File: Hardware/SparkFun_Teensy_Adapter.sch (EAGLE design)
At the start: 18 parts, among them J1 ARDUINO_R3_SHIELDUNO_R3_SHIEL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, J2 AVR_SPI_PRG_6PTH, U1 TEENSY-3.1

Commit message: Adding switch for USB Host, RTC battery holder
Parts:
- removed J2: AVR_SPI_PRG_6PTH, SparkFun-Connectors:AVR_SPI_PRG_6PTH
- removed U2: (no value), SparkFun-PowerIC:MIC52055V
- added BAT1: (no value), SparkFun-Electromechanical:BATTERY12PTH
- added C2: 100uF, SparkFun-Capacitors:100UF6.3V20%(1210)
- added JP1: M02PTH, SparkFun-Connectors:M02PTH
- added JP11: TEENSY-3.1, Testing:TEENSY-3.1
- added S1: (no value), SparkFun-Electromechanical:SWITCH-SPDTPTH
- JP9: value (none) -> AVR_SPI_PRG_6PTH; device SparkFun-Connectors:M03PTH -> SparkFun-Connectors:AVR_SPI_PRG_6PTH
- U1: value TEENSY-3.1 -> (none); device Testing:TEENSY-3.1 -> SparkFun-PowerIC:MIC52055V
- renumbered J1 to JP10
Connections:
- new net N$1: C2.1, S1.S
- net 3.3V: now also JP11.3.3V, JP9.2; no longer J2.2, U1.3.3V
- net 5V: now also JP11.VIN, U1.OUT; no longer U1.VIN, U2.OUT
- net A0: now also JP11.A0/14; no longer U1.A0/14
- net A1: now also JP11.A1/15; no longer U1.A1/15
- net A10: now also JP11.A10; no longer U1.A10
- net A11: now also JP11.A11; no longer U1.A11
- net A14/DAC: now also JP11.A14/DAC, JP8.2; no longer JP8.4, U1.A14/DAC
- net A2: now also JP11.A2/16; no longer U1.A2/16
- net A3: now also JP11.A3/17; no longer U1.A3/17
- net A6: now also JP11.A6/20*; no longer U1.A6/20*
- net A7: now also JP11.A7/21*; no longer U1.A7/21*
- net A8: now also JP11.A8/22*; no longer U1.A8/22*
- net A9: now also JP11.A9/23*; no longer U1.A9/23*
- net AREF: now also JP1.2, JP11.AREF; no longer JP9.3, U1.AREF
- net CS: now also JP11.10*/TX2/CS; no longer U1.10*/TX2/CS
- net D2: now also JP11.2; no longer U1.2
- net D3: now also JP11.3*; no longer U1.3*
- net D4: now also JP11.4*; no longer U1.4*
- net D5: now also JP11.5*; no longer U1.5*
- net D6: now also JP11.6*; no longer U1.6*
- net D7: now also JP11.7/RX3; no longer U1.7/RX3
- net D8: now also JP11.8/TX3; no longer U1.8/TX3
- net D9: now also JP11.9*/RX2; no longer U1.9*/RX2
- net GND: now also BAT1.+, C2.2, JP1.1, JP11.AGND, JP11.GND, JP11.GND1, JP8.4, JP9.6; no longer J2.6, JP9.1, U1.AGND, U1.GND1, U2.GND
- net MISO: now also JP11.12/DIN, JP9.1; no longer J2.1, U1.12/DIN
- net MOSI: now also JP11.11/DOUT, JP9.4; no longer J2.4, U1.11/DOUT
- net PROG: now also JP11.PROG; no longer U1.PROG
- net RESET: now also JP9.5; no longer J2.5
- net RTC_BATT: now also BAT1.-, JP11.VBAT; no longer JP8.2, U1.VBAT
- net RX: now also JP11.0/RX1; no longer U1.0/RX1
- net SCK: now also JP11.13/SCK, JP9.3; no longer J2.3, U1.13/SCK
- net SCL: now also JP11.A5/19/SCL0; no longer U1.A5/19/SCL0
- net SDA: now also JP11.A4/18/SDA0; no longer U1.A4/18/SDA0
- net TX: now also JP11.1/TX1; no longer U1.1/TX1
- net VRAW: now also U1.EN, U1.IN; no longer U2.EN, U2.IN
- net VUSB: now also JP11.VUSB, S1.P; no longer JP9.2, U1.VUSB
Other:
- note added: "ADC/PROG"
- note added: "RTC Battery"
- note added: "Switch to select USB Host mode"
- note added: "VBUS"
- note removed: "AREF/VBUS"
- note removed: "Add 100uF Cap for USB Host applications."
- note removed: "RTC Clock/ADC/PROG"
- moved on the sheet: C1, JP2, JP3

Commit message: Swapping to all PTH parts, fixing name silk
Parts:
- C1: device SparkFun-Capacitors:10UF-16V-10%(TANT) -> SparkFun-Capacitors:10UF-25V-20%(PTH)
- C2: device SparkFun-Capacitors:100UF6.3V20%(1210) -> SparkFun-Capacitors:100UF-25V-20%(PTH)
- U1: value (none) -> 5V; device SparkFun-PowerIC:MIC52055V -> SparkFun-PowerIC:V_REG_78XX-TO-220
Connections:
- net GND: now also C2.-; no longer C2.2
- net N$1: now also C2.+; no longer C2.1
- net VRAW: no longer U1.EN
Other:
- note added: "Toni Klopfenstein"
- note added: "v01"
- note removed: "5V"
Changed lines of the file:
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@@
 <layer number="223" name="223bmp" color="24" fill="1" visible="no" active="no"/>
 <layer number="224" name="224bmp" color="25" fill="1" visible="no" active="no"/>
+<layer number="225" name="225bmp" color="7" fill="1" visible="yes" active="yes"/>
+<layer number="226" name="226bmp" color="7" fill="1" visible="yes" active="yes"/>
+<layer number="227" name="227bmp" color="7" fill="1" visible="yes" active="yes"/>
+<layer number="228" name="228bmp" color="7" fill="1" visible="yes" active="yes"/>
+<layer number="229" name="229bmp" color="7" fill="1" visible="yes" active="yes"/>
+<layer number="230" name="230bmp" color="7" fill="1" visible="yes" active="yes"/>
+<layer number="231" name="231bmp" color="7" fill="1" visible="yes" active="yes"/>
 <layer number="248" name="Housing" color="7" fill="1" visible="yes" active="yes"/>
 <layer number="249" name="Edge" color="7" fill="1" visible="yes" active="yes"/>
@@
 <layer number="255" name="routoute" color="7" fill="1" visible="yes" active="yes"/>
 </layers>
-<schematic xreflabel="%F%N/%S" xrefpart="/%S.%C%R">
+<schematic xreflabel="%F%N/%S" xrefpart="/%S">
 <attributes>
 </attributes>
@@
 <part name="JP2" library="SparkFun-Connectors" deviceset="POWER_JACK" device="PTH_LOCK"/>
 <part name="GND5" library="SparkFun-Aesthetics" deviceset="GND" device=""/>
-<part name="U1" library="SparkFun-PowerIC" deviceset="MIC5205" device="5V"/>
 <part name="JP3" library="SparkFun-Connectors" deviceset="M02" device="JST-PTH-2"/>
 <part name="GND6" library="SparkFun-Aesthetics" deviceset="GND" device=""/>
 <part name="GND7" library="SparkFun-Aesthetics" deviceset="GND" device=""/>
-<part name="C1" library="SparkFun-Capacitors" deviceset="10UF-16V-10%(TANT)" device="" value="10uF"/>
+<part name="C1" library="SparkFun-Capacitors" deviceset="10UF-25V-20%(PTH)" device="" value="10uF"/>
 <part name="GND8" library="SparkFun-Aesthetics" deviceset="GND" device=""/>
 <part name="JP6" library="SparkFun-Connectors" deviceset="M02" device="PTH"/>
@@
 <part name="GND10" library="SparkFun-Aesthetics" deviceset="GND" device=""/>
 <part name="S1" library="SparkFun-Electromechanical" deviceset="SWITCH-SPDT" device="PTH"/>
-<part name="C2" library="SparkFun-Capacitors" deviceset="100UF6.3V20%(1210)" device="" value="100uF"/>
+<part name="U1" library="SparkFun-PowerIC" deviceset="V_REG_78XX" device="-TO-220" value="5V"/>
+<part name="C2" library="SparkFun-Capacitors" deviceset="100UF-25V-20%(PTH)" device="" value="100uF"/>
 </parts>
 <sheets>
@@
 <plain>
 <text x="10.16" y="157.48" size="1.778" layer="97">Input Voltage: 4-12V</text>
-<text x="76.2" y="139.7" size="1.778" layer="97">5V</text>
 <text x="218.44" y="182.88" size="1.27" layer="97">Switch to select USB Host mode</text>
 <text x="152.4" y="154.94" size="1.4224" layer="97">Add 32.768kHZ crystal to Teensy for use of RTC.  </text>
@@
 <wire x1="106.68" y1="185.42" x2="106.68" y2="127" width="0.2032" layer="97" style="shortdash"/>
 <text x="116.84" y="129.54" size="2.54" layer="97">RTC Battery</text>
+<text x="241.3" y="7.62" size="2.54" layer="94">v01</text>
+<text x="167.64" y="10.16" size="2.54" layer="94">Toni Klopfenstein</text>
 </plain>
 <instances>
@@
 </instance>
 <instance part="GND5" gate="1" x="40.64" y="137.16"/>
-<instance part="U1" gate="G$1" x="78.74" y="149.86"/>
 <instance part="JP3" gate="G$1" x="10.16" y="170.18" smashed="yes">
 <attribute name="NAME" x="7.62" y="176.022" size="1.778" layer="95"/>
 </instance>
 <instance part="GND6" gate="1" x="20.32" y="165.1"/>
-<instance part="GND7" gate="1" x="63.5" y="137.16"/>
+<instance part="GND7" gate="1" x="81.28" y="137.16"/>
 <instance part="C1" gate="G$1" x="50.8" y="149.86"/>
 <instance part="GND8" gate="1" x="50.8" y="137.16"/>
@@
 <instance part="GND10" gate="1" x="129.54" y="17.78"/>
 <instance part="S1" gate="1" x="213.36" y="177.8"/>
-<instance part="C2" gate="G$1" x="220.98" y="165.1"/>
+<instance part="U1" gate="G$1" x="81.28" y="154.94"/>
+<instance part="C2" gate="G$1" x="220.98" y="167.64"/>
 </instances>
 <busses>
@@
 </segment>
 <segment>
-<pinref part="U1" gate="G$1" pin="GND"/>
-<wire x1="68.58" y1="149.86" x2="63.5" y2="149.86" width="0.1524" layer="91"/>
-<wire x1="63.5" y1="149.86" x2="63.5" y2="139.7" width="0.1524" layer="91"/>
-<pinref part="GND7" gate="1" pin="GND"/>
-</segment>
-<segment>
 <pinref part="C1" gate="G$1" pin="-"/>
 <pinref part="GND8" gate="1" pin="GND"/>
@@
 <pinref part="GND11" gate="1" pin="GND"/>
 <wire x1="220.98" y1="162.56" x2="220.98" y2="160.02" width="0.1524" layer="91"/>
-<pinref part="C2" gate="G$1" pin="2"/>
+<pinref part="C2" gate="G$1" pin="-"/>
+</segment>
+<segment>
+<pinref part="GND7" gate="1" pin="GND"/>
+<wire x1="81.28" y1="144.78" x2="81.28" y2="142.24" width="0.1524" layer="91"/>
+<pinref part="U1" gate="G$1" pin="GND"/>
+<wire x1="81.28" y1="142.24" x2="81.28" y2="139.7" width="0.1524" layer="91"/>
+<wire x1="81.28" y1="147.32" x2="81.28" y2="144.78" width="0.1524" layer="91"/>
 </segment>
 </net>
@@
 <segment>
 <pinref part="JP2" gate="G$1" pin="PWR"/>
-<pinref part="U1" gate="G$1" pin="IN"/>
 <wire x1="22.86" y1="154.94" x2="50.8" y2="154.94" width="0.1524" layer="91"/>
-<pinref part="U1" gate="G$1" pin="EN"/>
-<wire x1="50.8" y1="154.94" x2="60.96" y2="154.94" width="0.1524" layer="91"/>
-<wire x1="60.96" y1="154.94" x2="68.58" y2="154.94" width="0.1524" layer="91"/>
-<wire x1="68.58" y1="144.78" x2="60.96" y2="144.78" width="0.1524" layer="91"/>
-<wire x1="60.96" y1="144.78" x2="60.96" y2="154.94" width="0.1524" layer="91"/>
-<junction x="60.96" y="154.94"/>
+<wire x1="50.8" y1="154.94" x2="73.66" y2="154.94" width="0.1524" layer="91"/>
 <pinref part="C1" gate="G$1" pin="+"/>
 <wire x1="50.8" y1="152.4" x2="50.8" y2="154.94" width="0.1524" layer="91"/>
 <junction x="50.8" y="154.94"/>
+<pinref part="U1" gate="G$1" pin="IN"/>
 </segment>
 </net>
@@
 </segment>
 <segment>
-<pinref part="U1" gate="G$1" pin="OUT"/>
-<wire x1="86.36" y1="154.94" x2="91.44" y2="154.94" width="0.1524" layer="91"/>
-<label x="91.44" y="154.94" size="1.27" layer="95" xref="yes"/>
-</segment>
-<segment>
 <pinref part="JP10" gate="G$1" pin="5V"/>
 <wire x1="63.5" y1="86.36" x2="55.88" y2="86.36" width="0.1524" layer="91"/>
 <label x="55.88" y="86.36" size="1.27" layer="95" rot="R180" xref="yes"/>
+</segment>
+<segment>
+<wire x1="96.52" y1="154.94" x2="99.06" y2="154.94" width="0.1524" layer="91"/>
+<label x="101.6" y="154.94" size="1.27" layer="95" xref="yes"/>
+<pinref part="U1" gate="G$1" pin="OUT"/>
+<wire x1="99.06" y1="154.94" x2="101.6" y2="154.94" width="0.1524" layer="91"/>
+<wire x1="88.9" y1="154.94" x2="96.52" y2="154.94" width="0.1524" layer="91"/>
 </segment>
 </net>
@@
 <wire x1="218.44" y1="175.26" x2="220.98" y2="175.26" width="0.1524" layer="91"/>
 <wire x1="220.98" y1="175.26" x2="220.98" y2="170.18" width="0.1524" layer="91"/>
-<pinref part="C2" gate="G$1" pin="1"/>
-</segment>
-</net>
+<pinref part="C2" gate="G$1" pin="+"/>
+</segment>
+</net>

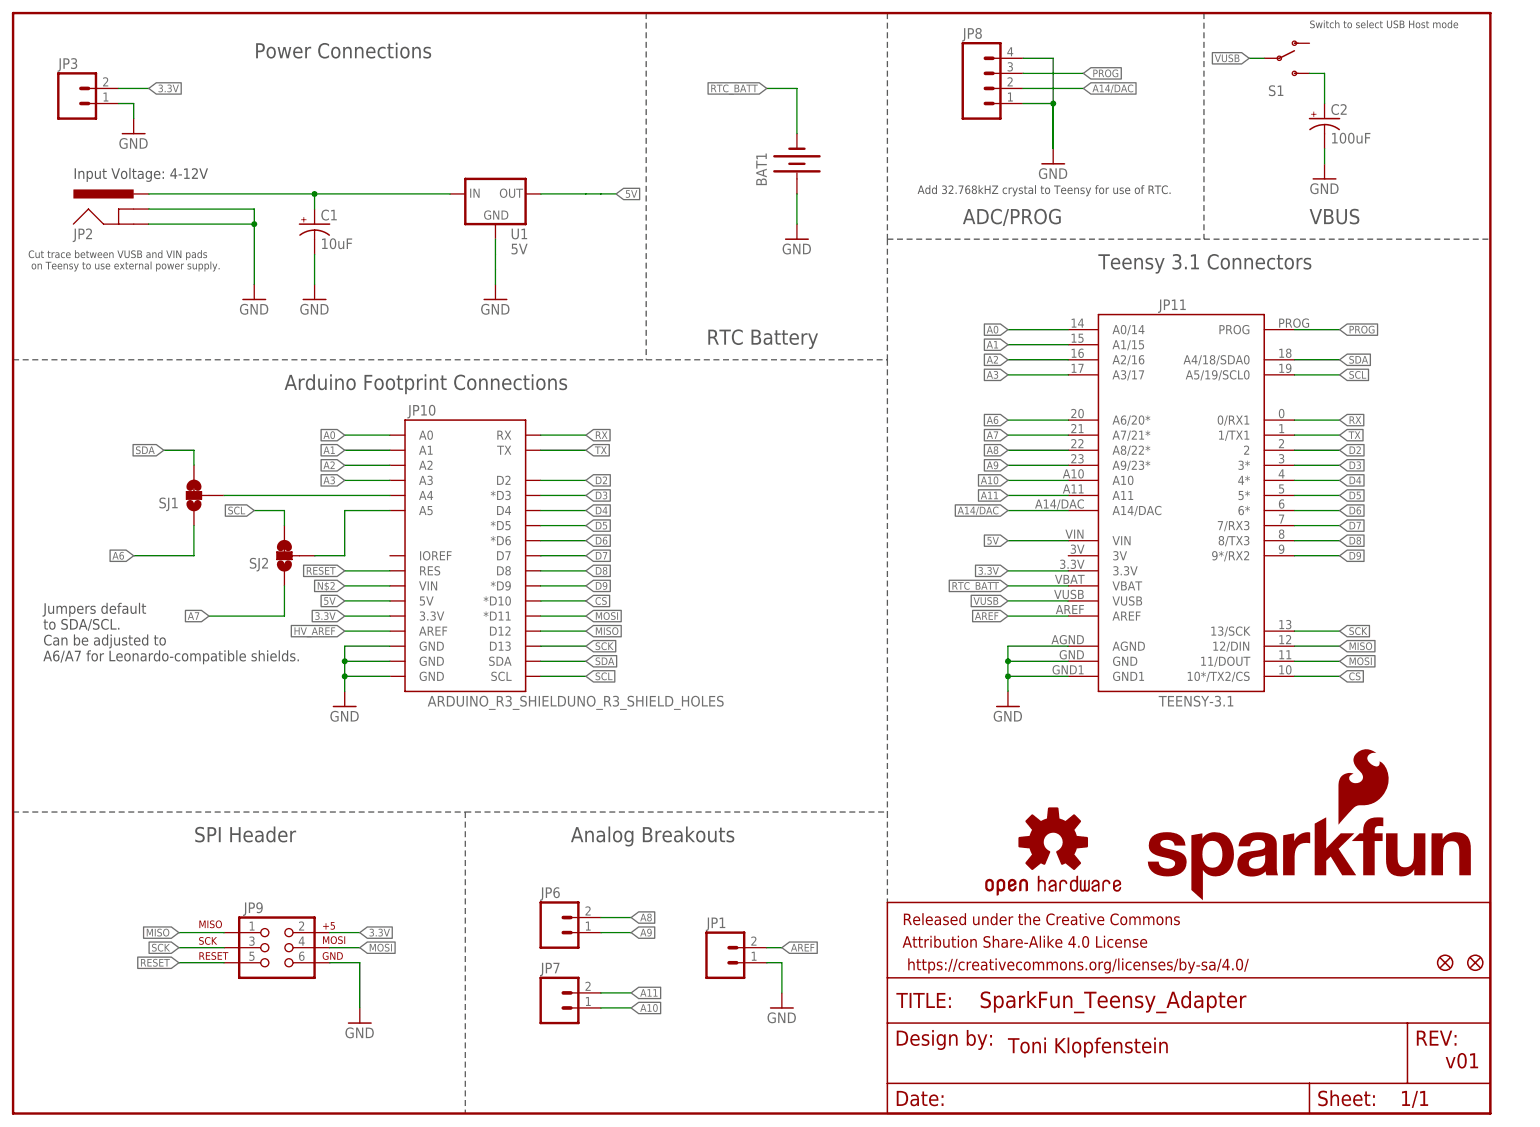
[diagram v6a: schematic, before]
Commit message: Fixing QC checklist issues
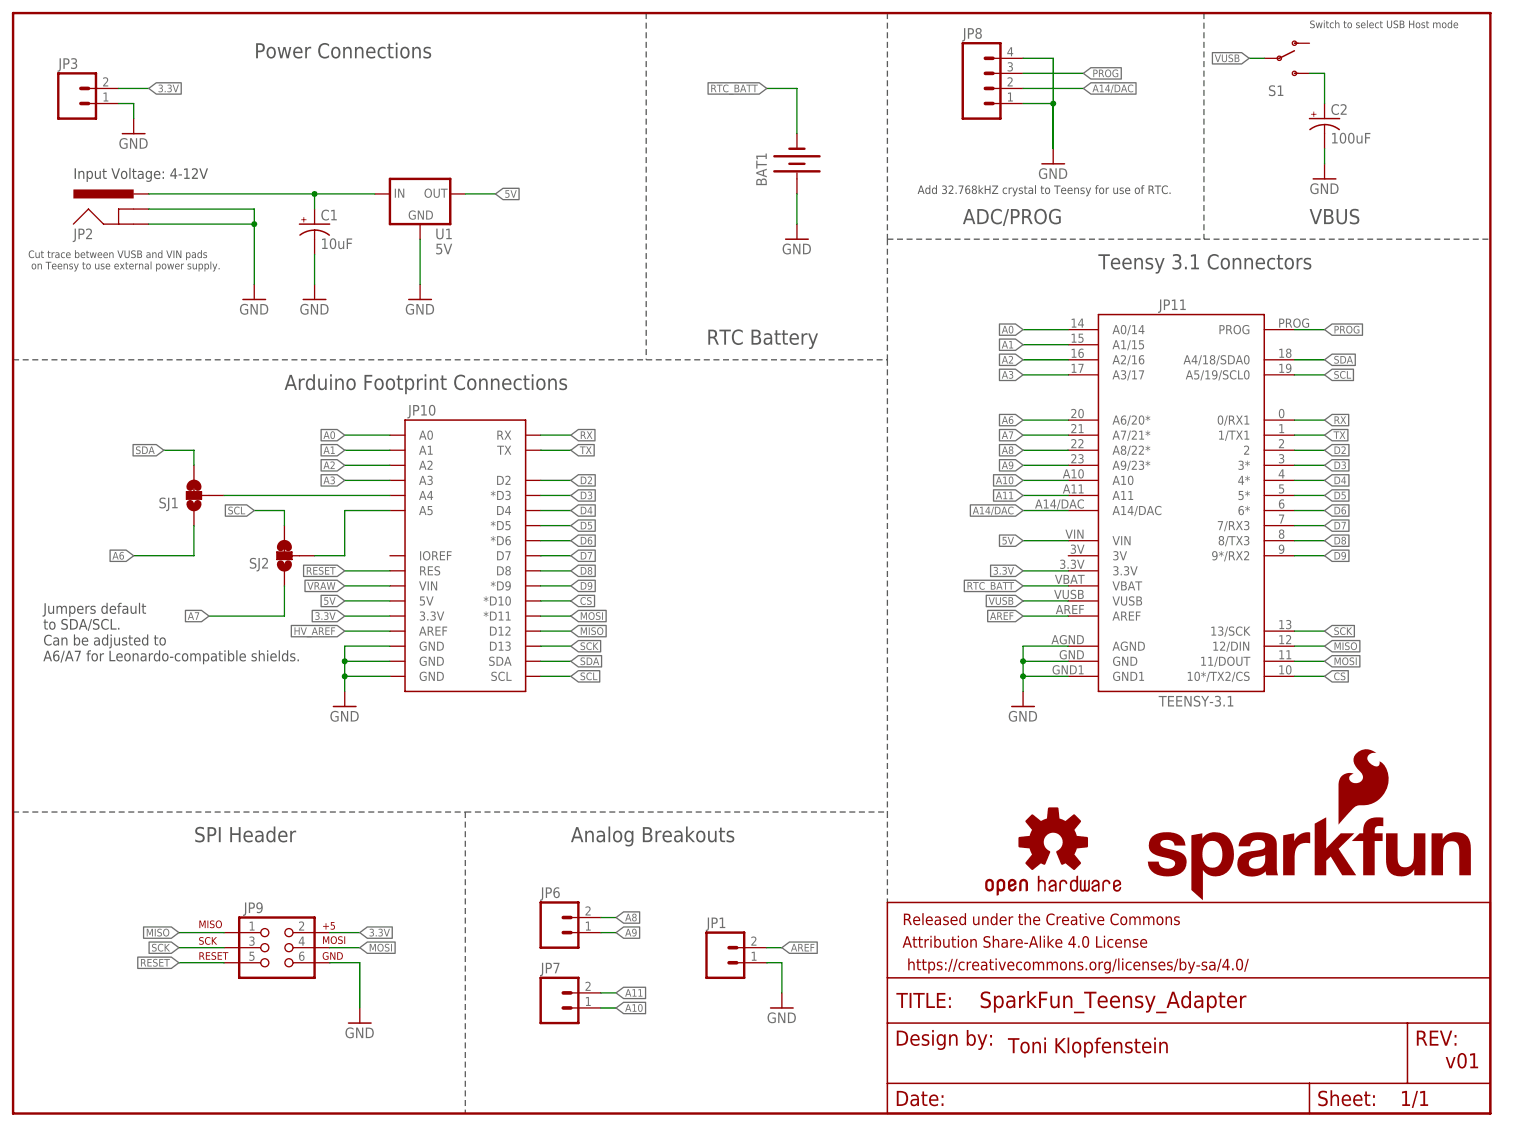
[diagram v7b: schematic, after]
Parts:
- removed FID1, FID2: FIDUCIAL1X2, SparkFun-Aesthetics:FIDUCIAL1X2
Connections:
- removed net N$2: JP10.VIN
- net VRAW: now also JP10.VIN
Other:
- moved on the sheet: U1

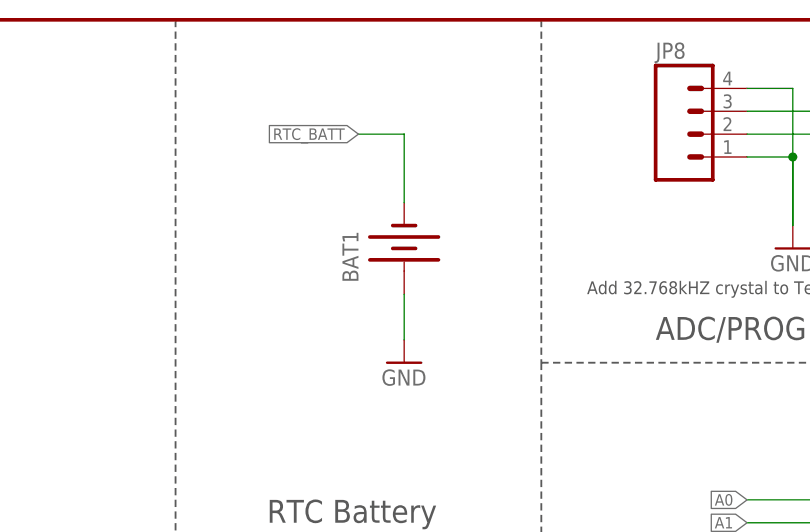
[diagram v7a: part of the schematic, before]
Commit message: Fixing battery connections
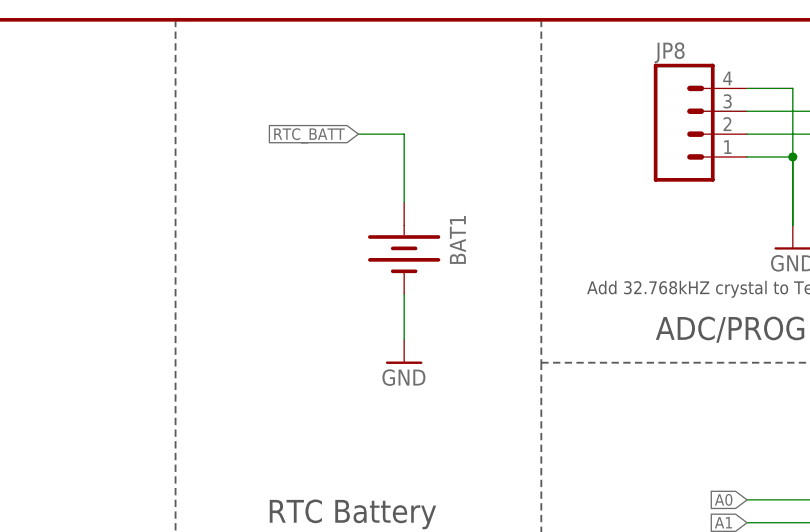
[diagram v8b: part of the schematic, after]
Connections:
- net GND: now also BAT1.-; no longer BAT1.+
- net RTC_BATT: now also BAT1.+; no longer BAT1.-
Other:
- moved on the sheet: BAT1
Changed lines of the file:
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@@
 <instance part="GND9" gate="1" x="175.26" y="160.02"/>
 <instance part="GND11" gate="1" x="220.98" y="157.48"/>
-<instance part="BAT1" gate="G$1" x="132.08" y="160.02" rot="R90"/>
+<instance part="BAT1" gate="G$1" x="132.08" y="160.02" rot="R270"/>
 <instance part="GND4" gate="1" x="132.08" y="147.32"/>
 <instance part="JP1" gate="G$1" x="119.38" y="25.4" smashed="yes">
@@
 </segment>
 <segment>
-<pinref part="BAT1" gate="G$1" pin="+"/>
-<pinref part="GND4" gate="1" pin="GND"/>
-<wire x1="132.08" y1="154.94" x2="132.08" y2="149.86" width="0.1524" layer="91"/>
-</segment>
-<segment>
 <pinref part="JP1" gate="G$1" pin="1"/>
 <wire x1="127" y1="25.4" x2="129.54" y2="25.4" width="0.1524" layer="91"/>
@@
 <pinref part="U1" gate="G$1" pin="GND"/>
 <wire x1="68.58" y1="147.32" x2="68.58" y2="139.7" width="0.1524" layer="91"/>
+</segment>
+<segment>
+<pinref part="BAT1" gate="G$1" pin="-"/>
+<pinref part="GND4" gate="1" pin="GND"/>
+<wire x1="132.08" y1="154.94" x2="132.08" y2="149.86" width="0.1524" layer="91"/>
 </segment>
 </net>
@@
 </segment>
 <segment>
-<pinref part="BAT1" gate="G$1" pin="-"/>
-<wire x1="132.08" y1="165.1" x2="132.08" y2="172.72" width="0.1524" layer="91"/>
 <wire x1="132.08" y1="172.72" x2="127" y2="172.72" width="0.1524" layer="91"/>
 <label x="127" y="172.72" size="1.27" layer="95" rot="R180" xref="yes"/>
-</segment>
-</net>
+<pinref part="BAT1" gate="G$1" pin="+"/>
+<wire x1="132.08" y1="165.1" x2="132.08" y2="172.72" width="0.1524" layer="91"/>
+</segment>
+</net>
